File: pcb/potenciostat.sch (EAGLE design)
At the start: 25 parts, among them IC3 TL074P, K2 ZNS5406, Q1 2N3904

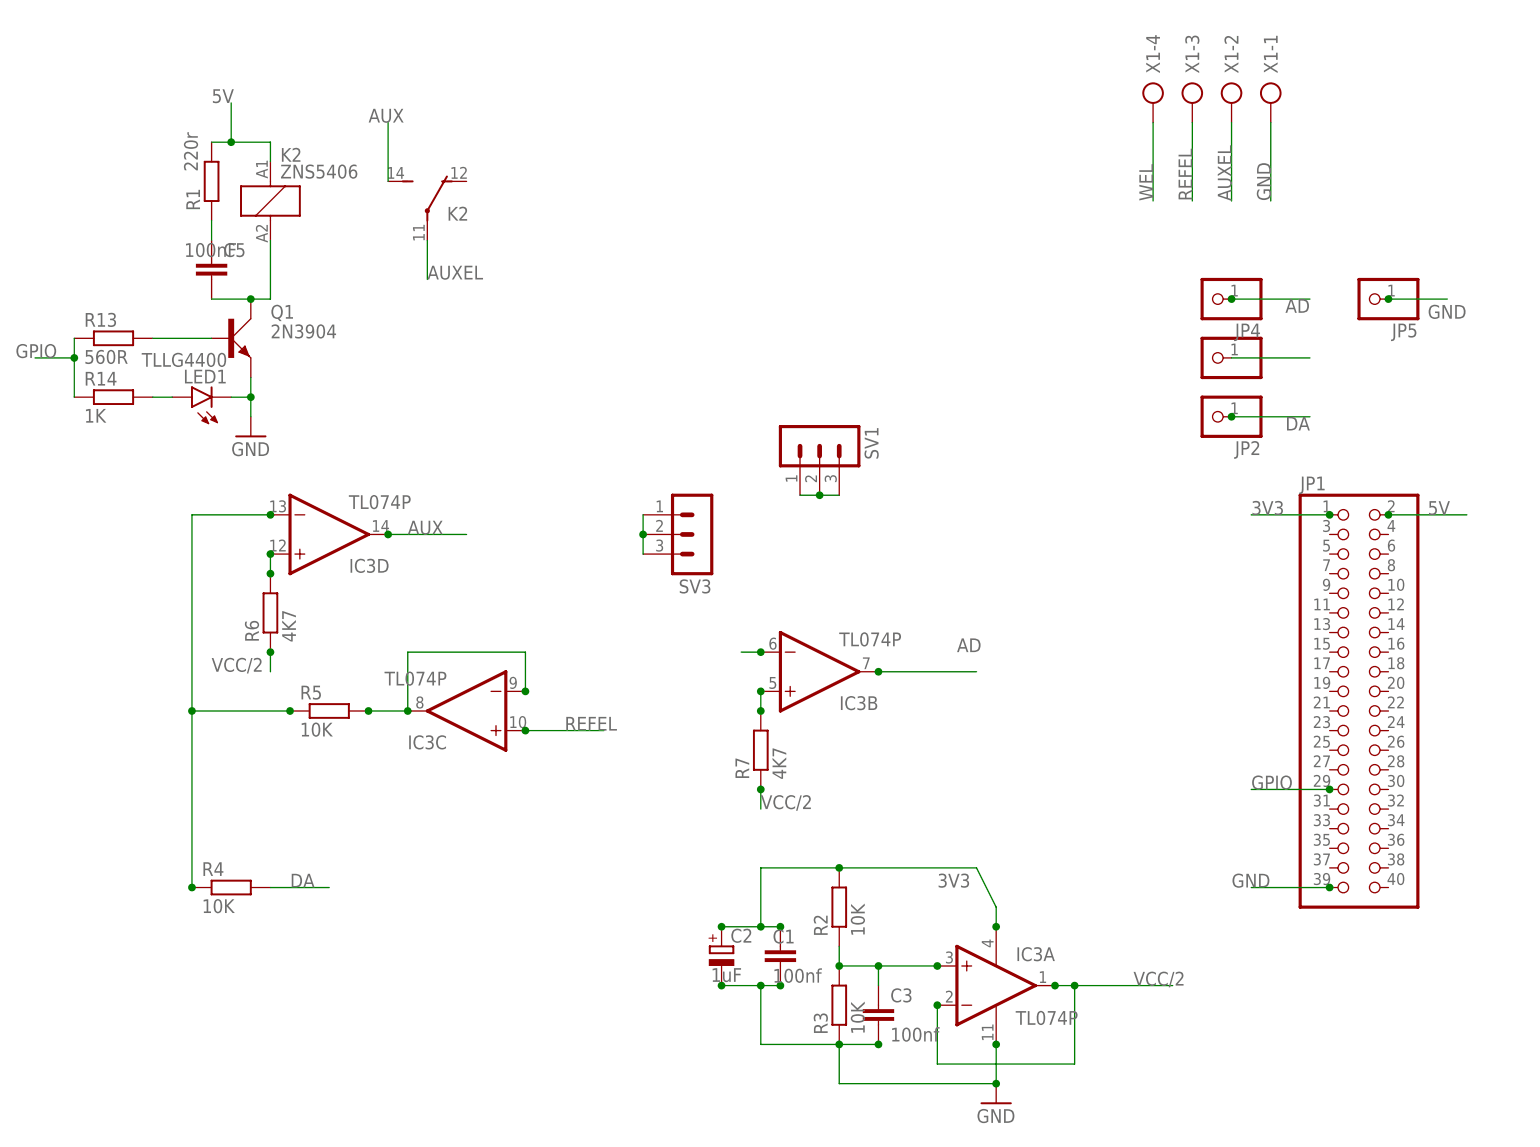
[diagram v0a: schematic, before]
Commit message: Remove prints and add docstrings
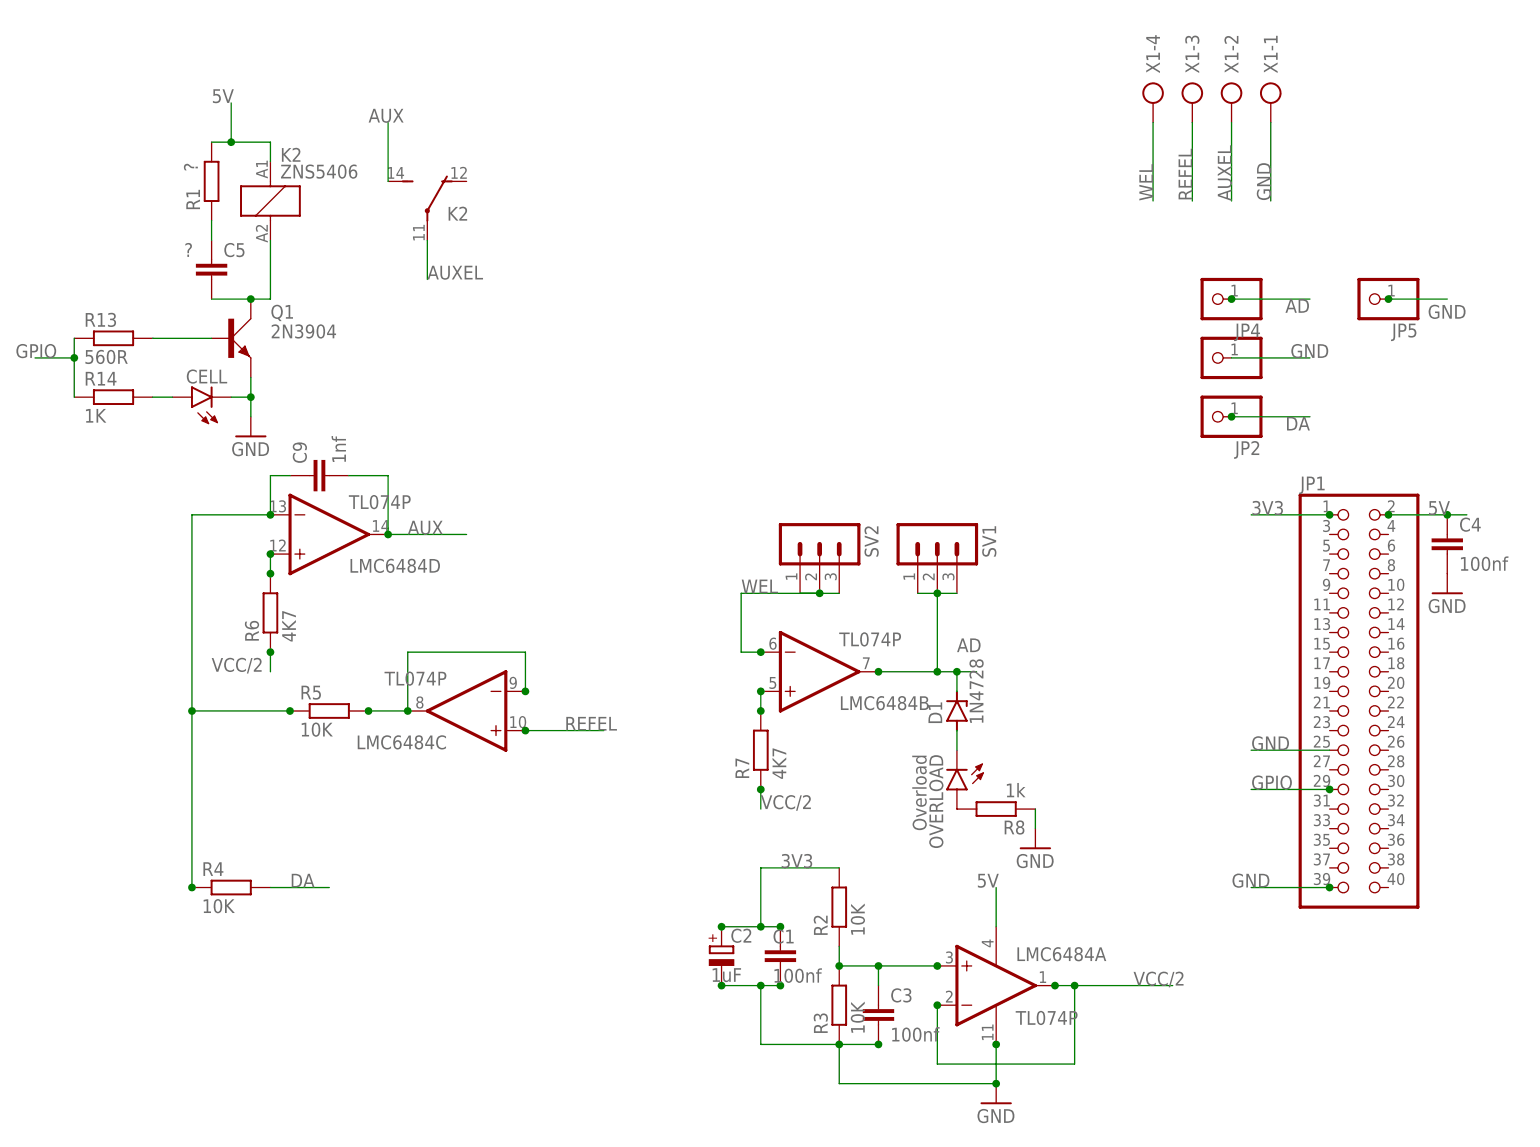
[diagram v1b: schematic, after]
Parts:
- removed SV3: (no value), con-lstb:MA03-1
- added C4: 100nf, rcl:C-EU050-035X075
- added C9: 1nf, rcl:C-EU050-035X075
- added D1: 1N4728, diode:1N4728
- added OVERLOAD: Overload, led:TLLG4400
- added R8: 1k, rcl:R-EU_0207/7
- added SV2: (no value), con-lstb:MA03-1
- C5: value 100nF -> ?
- R1: value 220r -> ?
- renumbered IC3 to LMC6484, LED1 to CELL
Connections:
- removed net N$7: JP3.1
- removed net N$9: SV3.1, SV3.2, SV3.3
- net 3V3: no longer LMC6484P.V+
- net 5V: now also C4.1, LMC6484P.V+
- net AD: now also D1.C, SV1.1, SV1.2, SV1.3
- net AUX: now also C9.2
- net GND: now also C4.2, JP1.25, JP3.1, R8.1
- net N$1: now also OVERLOAD.A, R8.2; no longer LMC6484B.-IN
- net N$10: now also D1.A, OVERLOAD.C; no longer SV1.1, SV1.2, SV1.3
- net N$4: now also C9.1
- net WEL: now also LMC6484B.-IN, SV2.1, SV2.2, SV2.3
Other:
- moved on the sheet: SV1

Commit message: Placa com seleção ganho
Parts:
- removed SV1, SV2: (no value), con-lstb:MA03-1
- added C10, C6, C7, C8: 1uF, rcl:C-EU050-035X075
- added R10: 47K, rcl:R-EU_0207/7
- added R11: 4K7, rcl:R-EU_0207/7
- added R12: 470, rcl:R-EU_0207/7
- added R9: 470K, rcl:R-EU_0207/7
- added SW1: (no value), special:SW_DIP-6
- Q1: value 2N3904 -> BC548; device transistor-small-signal:2N3904 -> transistor-npn:BC548
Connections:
- new net N$11: C8.2, R11.1, SW1.2
- new net N$12: C10.2, R10.1, SW1.3
- new net N$13: C6.2, R9.1, SW1.4
- new net N$7: C7.2, R12.1, SW1.1
- new net N$9: SW1.10, SW1.11, SW1.12, SW1.8, SW1.9
- net AD: now also SW1.5, SW1.6; no longer SV1.1, SV1.2, SV1.3
- net WEL: now also C10.1, C6.1, C7.1, C8.1, R10.2, R11.2, R12.2, R9.2, SW1.7; no longer SV2.1, SV2.2, SV2.3
